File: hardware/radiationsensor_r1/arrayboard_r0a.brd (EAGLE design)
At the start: 160 x 100 mm, 21 parts, among them CN0 RADIATION-SENSOR-REV1, CN1 RADIATION-SENSOR-REV1, CN10 RADIATION-SENSOR-REV1, CN11 RADIATION-SENSOR-REV1, CN12 RADIATION-SENSOR-REV1, CN13 RADIATION-SENSOR-REV1, CN14 RADIATION-SENSOR-REV1, CN15 RADIATION-SENSOR-REV1, CN2 RADIATION-SENSOR-REV1, CN3 RADIATION-SENSOR-REV1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

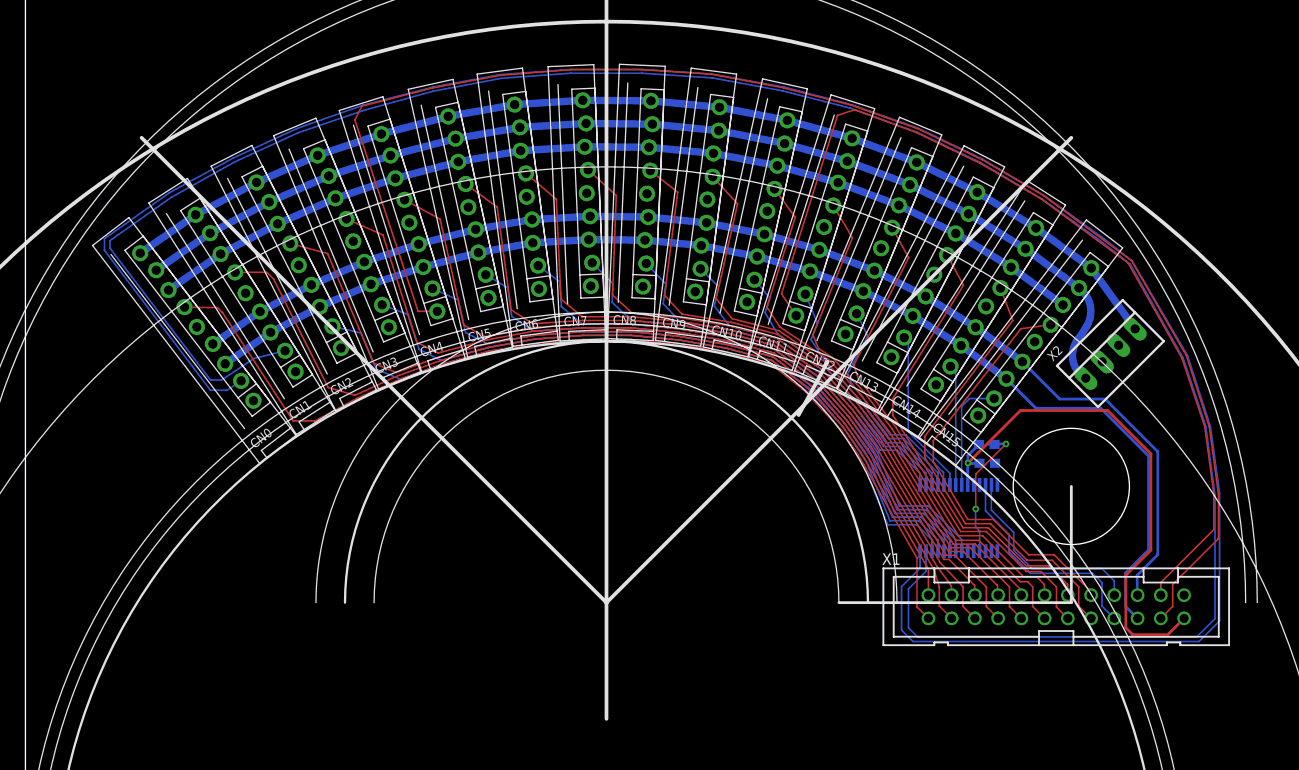
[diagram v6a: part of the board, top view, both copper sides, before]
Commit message: started board outline and ground plane
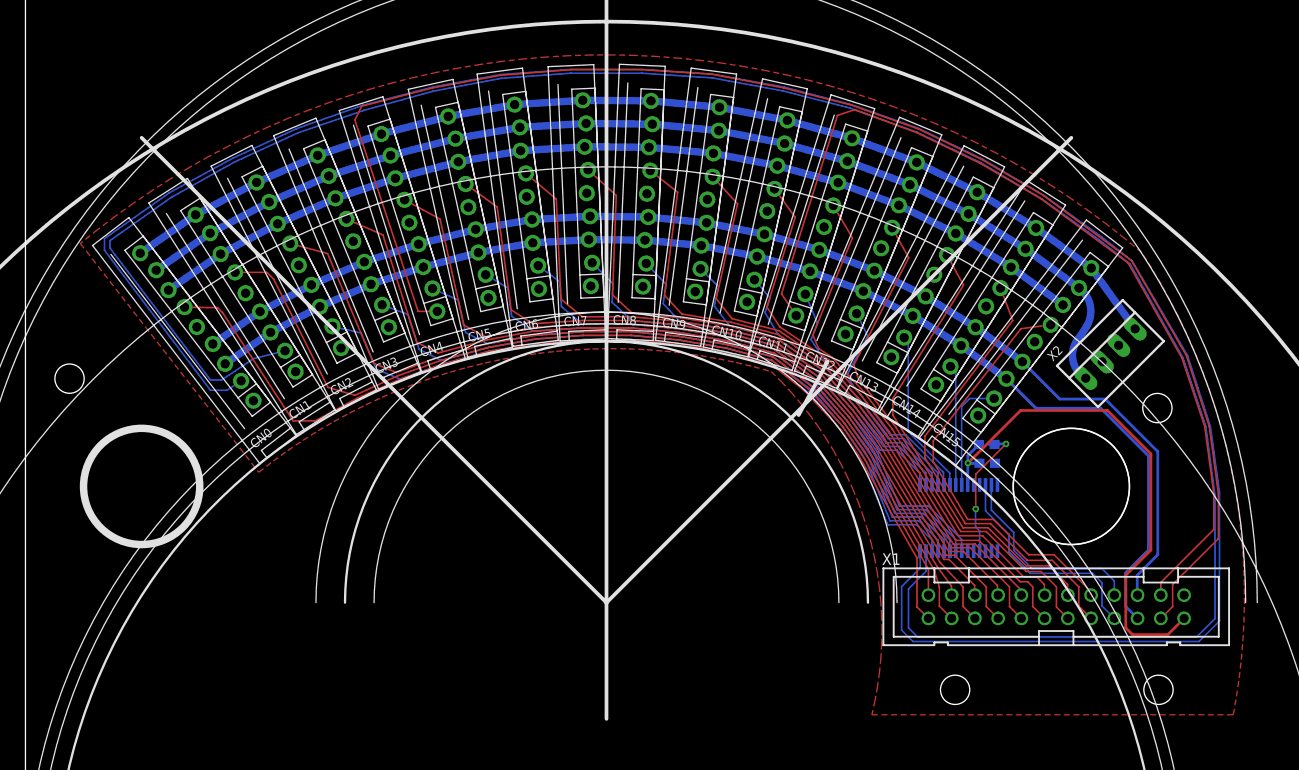
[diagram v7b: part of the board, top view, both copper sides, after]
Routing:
- added copper zone on layer 1, net GND
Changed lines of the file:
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@@
 <layer number="43" name="vRestrict" color="2" fill="10" visible="yes" active="yes"/>
 <layer number="44" name="Drills" color="7" fill="1" visible="no" active="yes"/>
-<layer number="45" name="Holes" color="7" fill="1" visible="no" active="yes"/>
+<layer number="45" name="Holes" color="7" fill="1" visible="yes" active="yes"/>
 <layer number="46" name="Milling" color="3" fill="1" visible="no" active="yes"/>
 <layer number="47" name="Measures" color="7" fill="1" visible="no" active="yes"/>
@@
 <wire x1="3.175" y1="0" x2="123.825" y2="0" width="0.254" layer="21" curve="-180"/>
 <wire x1="34.925" y1="31.75" x2="92.075" y2="31.75" width="0.254" layer="21" curve="-180"/>
-<wire x1="88.9" y1="31.75" x2="114.3" y2="31.75" width="0.3048" layer="21"/>
-<wire x1="114.3" y1="31.75" x2="114.3" y2="44.45" width="0.3048" layer="21"/>
 <circle x="114.3" y="44.45" radius="6.35" width="0.01" layer="20"/>
 <wire x1="87.6724" y1="58.0908" x2="84.5" y2="52.25" width="0.4064" layer="21"/>
 <circle x="114.3" y="44.45" radius="6.35" width="0.3048" layer="39"/>
 <circle x="114.3" y="44.45" radius="6.35" width="0.3048" layer="40"/>
+<circle x="12.7" y="44.45" radius="6.35" width="0.8128" layer="21"/>
+<hole x="101.6" y="22.225" drill="3.2"/>
+<hole x="123.825" y="22.225" drill="3.2"/>
+<hole x="123.70435" y="53.01615" drill="3.2"/>
+<hole x="4.81965" y="56.22925" drill="3.2"/>
+<circle x="114.3" y="44.45" radius="6.35" width="0.1778" layer="21"/>
 </plain>
 <attributes>
@@
 <contactref element="X2" pad="2"/>
 <contactref element="X2" pad="3"/>
-<wire x1="117.668915625" y1="58.07424375" x2="119.46496875" y2="59.870296875" width="0" layer="19" extent="1-1"/>
-<wire x1="113.39106875" y1="64.283903125" x2="119.46496875" y2="59.870296875" width="0" layer="19" extent="1-1"/>
-<wire x1="105.96" y1="46.988" x2="117.668915625" y2="58.07424375" width="0" layer="19" extent="16-16"/>
+<polygon width="0.1778" layer="1">
+<vertex x="6" y="71"/>
+<vertex x="25.5" y="46" curve="-55"/>
+<vertex x="81.5" y="57" curve="-60"/>
+<vertex x="92.5" y="19.5"/>
+<vertex x="132" y="19.5" curve="44"/>
+<vertex x="122" y="70" curve="80"/>
+</polygon>
 <wire x1="103.625" y1="44.625" x2="105.96" y2="46.988" width="0" layer="19" extent="16-16"/>
 <wire x1="104.925" y1="37.375" x2="103.625" y2="44.625" width="0" layer="19" extent="16-16"/>
 <wire x1="105.575" y1="37.375" x2="104.925" y2="37.375" width="0" layer="19" extent="16-16"/>
 <wire x1="106.225" y1="37.375" x2="105.575" y2="37.375" width="0" layer="19" extent="16-16"/>
-<wire x1="126.62" y1="32.57" x2="106.225" y2="37.375" width="0" layer="19" extent="16-16"/>
+<wire x1="117.668915625" y1="58.07424375" x2="105.96" y2="46.988" width="0" layer="19" extent="16-16"/>
 </signal>
 <signal name="5V">

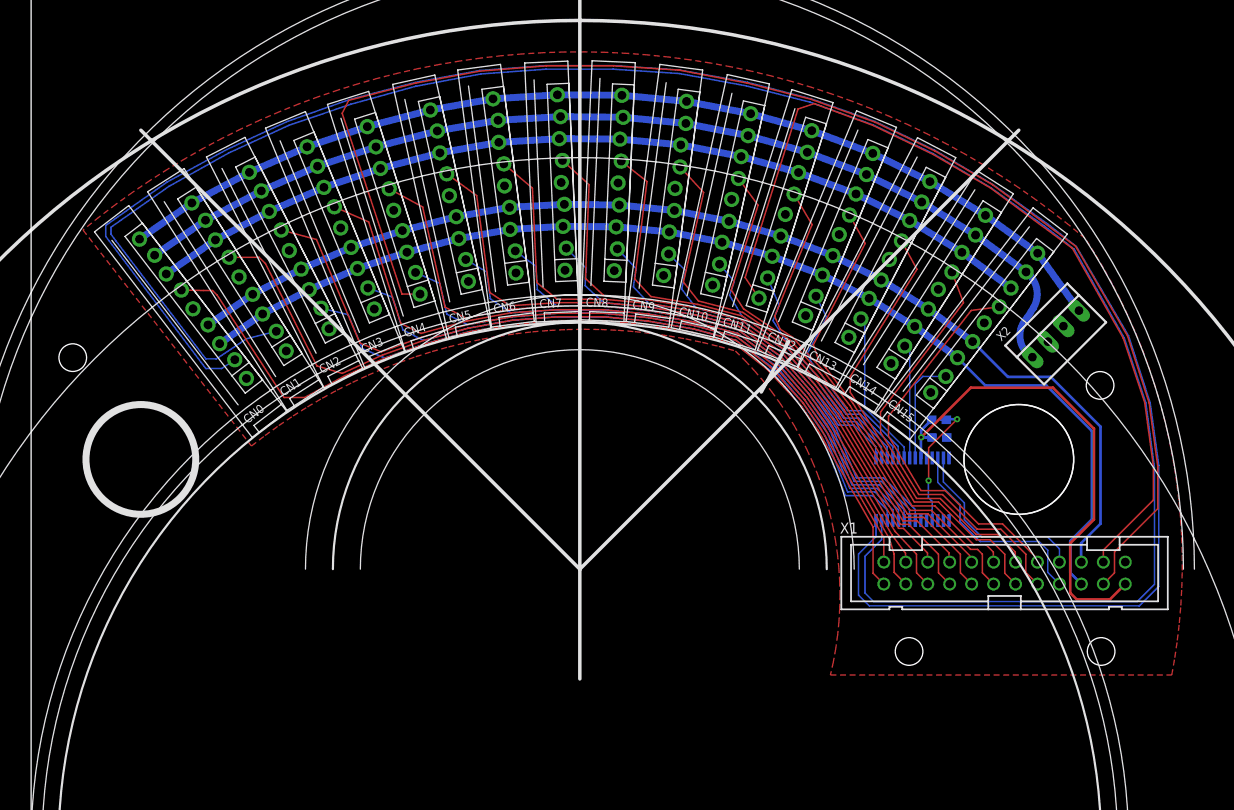
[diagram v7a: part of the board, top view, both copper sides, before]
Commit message: Board outline and ground planes complete
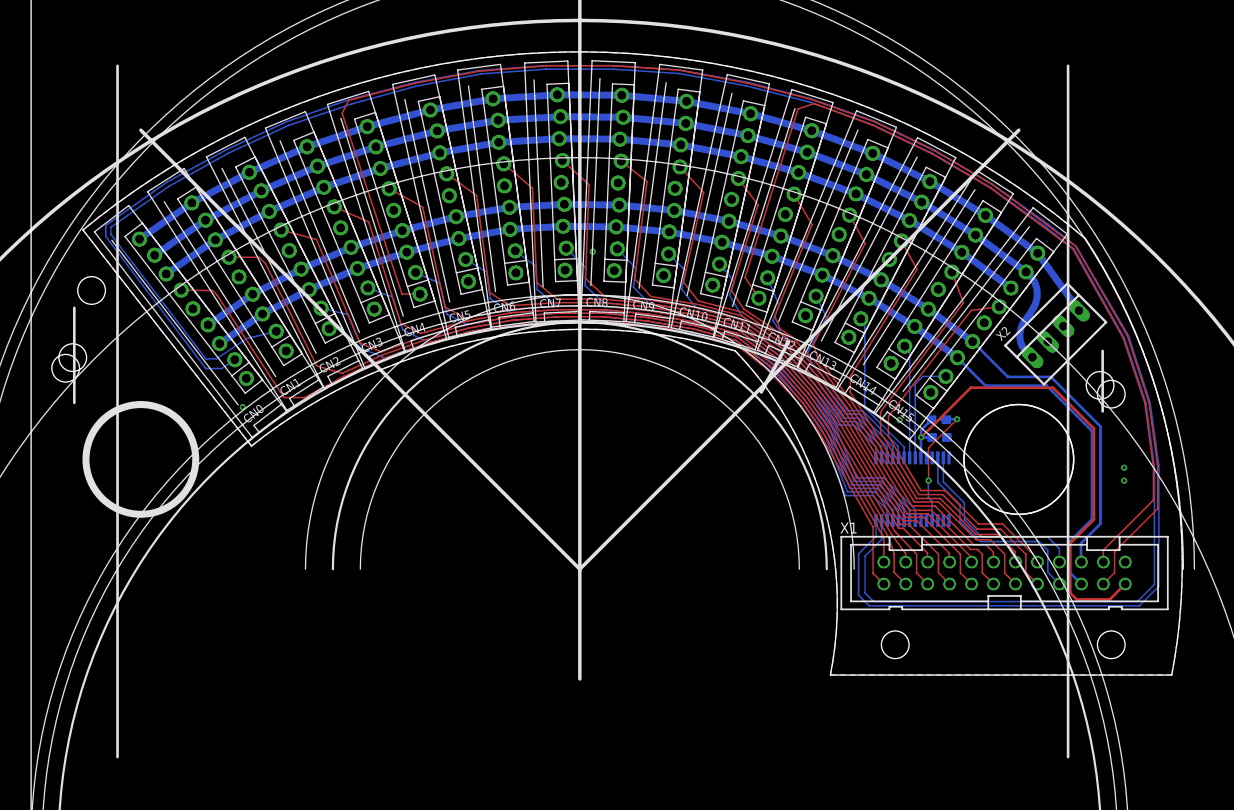
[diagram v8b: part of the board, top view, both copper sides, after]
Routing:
- net GND: vias 0 -> 5
- added copper zone on layer 16, net GND
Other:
- outline, holes or cut-outs redrawn
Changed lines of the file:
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@@
 <setting verticaltext="up"/>
 </settings>
-<grid distance="0.5" unitdist="mm" unit="mm" style="lines" multiple="1" display="yes" altdistance="0.025" altunitdist="inch" altunit="inch"/>
+<grid distance="1" unitdist="mm" unit="mm" style="lines" multiple="1" display="yes" altdistance="0.025" altunitdist="inch" altunit="inch"/>
 <layers>
 <layer number="1" name="Top" color="4" fill="1" visible="yes" active="yes"/>
@@
 <circle x="114.3" y="44.45" radius="6.35" width="0.3048" layer="40"/>
 <circle x="12.7" y="44.45" radius="6.35" width="0.8128" layer="21"/>
-<hole x="101.6" y="22.225" drill="3.2"/>
-<hole x="123.825" y="22.225" drill="3.2"/>
 <hole x="123.70435" y="53.01615" drill="3.2"/>
 <hole x="4.81965" y="56.22925" drill="3.2"/>
 <circle x="114.3" y="44.45" radius="6.35" width="0.1778" layer="21"/>
+<wire x1="6" y1="71" x2="25.5" y2="46" width="0.01" layer="20"/>
+<wire x1="25.5" y1="46" x2="81.5" y2="57" width="0.01" layer="20" curve="-55"/>
+<wire x1="81.5" y1="57" x2="92.5" y2="19.5" width="0.01" layer="20" curve="-55"/>
+<wire x1="92.5" y1="19.5" x2="132" y2="19.5" width="0.01" layer="20"/>
+<wire x1="132" y1="19.5" x2="122" y2="70" width="0.01" layer="20" curve="44"/>
+<wire x1="122" y1="70" x2="6" y2="71" width="0.01" layer="20" curve="80"/>
+<circle x="114.3" y="44.45" radius="6.35" width="0.3048" layer="40"/>
+<circle x="114.3" y="44.45" radius="6.35" width="0.3048" layer="40"/>
+<circle x="114.3" y="44.45" radius="6.35" width="0.3048" layer="42"/>
+<wire x1="120" y1="90" x2="120" y2="10" width="0.3048" layer="21"/>
+<wire x1="10" y1="90" x2="10" y2="10" width="0.3048" layer="21"/>
+<wire x1="5" y1="62" x2="5" y2="51" width="0.3048" layer="21"/>
+<wire x1="124" y1="57" x2="124" y2="50" width="0.3048" layer="21"/>
+<hole x="125" y="52" drill="3.2"/>
+<hole x="4" y="55" drill="3.2"/>
+<hole x="125" y="23" drill="3.2"/>
+<hole x="100" y="23" drill="3.2"/>
+<hole x="7" y="64" drill="3.2"/>
 </plain>
 <attributes>
@@
 <vertex x="6" y="71"/>
 <vertex x="25.5" y="46" curve="-55"/>
-<vertex x="81.5" y="57" curve="-60"/>
+<vertex x="81.5" y="57" curve="-55"/>
 <vertex x="92.5" y="19.5"/>
 <vertex x="132" y="19.5" curve="44"/>
 <vertex x="122" y="70" curve="80"/>
 </polygon>
-<wire x1="103.625" y1="44.625" x2="105.96" y2="46.988" width="0" layer="19" extent="16-16"/>
-<wire x1="104.925" y1="37.375" x2="103.625" y2="44.625" width="0" layer="19" extent="16-16"/>
-<wire x1="105.575" y1="37.375" x2="104.925" y2="37.375" width="0" layer="19" extent="16-16"/>
-<wire x1="106.225" y1="37.375" x2="105.575" y2="37.375" width="0" layer="19" extent="16-16"/>
-<wire x1="117.668915625" y1="58.07424375" x2="105.96" y2="46.988" width="0" layer="19" extent="16-16"/>
+<via x="126.5" y="42" extent="1-16" drill="0.3302"/>
+<polygon width="0.1778" layer="16">
+<vertex x="6" y="71"/>
+<vertex x="25.5" y="46" curve="-55"/>
+<vertex x="81.5" y="57" curve="-55"/>
+<vertex x="92.5" y="19.5"/>
+<vertex x="132" y="19.5" curve="44"/>
+<vertex x="122" y="70" curve="80"/>
+</polygon>
+<via x="24.5" y="50.5" extent="1-16" drill="0.3302"/>
+<via x="65" y="68.5" extent="1-16" drill="0.3302"/>
+<via x="100.5" y="49" extent="1-16" drill="0.3302"/>
+<via x="126.5" y="43.5" extent="1-16" drill="0.3302"/>
 </signal>
 <signal name="5V">
